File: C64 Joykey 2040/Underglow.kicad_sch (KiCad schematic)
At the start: 19 parts, among them J3 LED_EN, Q1 2N3904

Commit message: First layout drafted
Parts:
- J3: footprint TestPoint:TestPoint_Pad_D1.0mm -> TestPoint:TestPoint_THTPad_D1.5mm_Drill0.7mm
- Q1: footprint 2n3904:2N3904_TO-92_Horizontal_FlatSideDown -> Package_TO_SOT_THT:TO-92_Inline_Wide
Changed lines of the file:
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@@
 			)
 		)
-		(property "Footprint" "2n3904:2N3904_TO-92_Horizontal_FlatSideDown"
+		(property "Footprint" "Package_TO_SOT_THT:TO-92_Inline_Wide"
 			(at 186.69 109.855 0)
 			(effects
@@
 			)
 		)
-		(property "Footprint" "TestPoint:TestPoint_Pad_D1.0mm"
+		(property "Footprint" "TestPoint:TestPoint_THTPad_D1.5mm_Drill0.7mm"
 			(at 217.17 107.95 0)
 			(effects

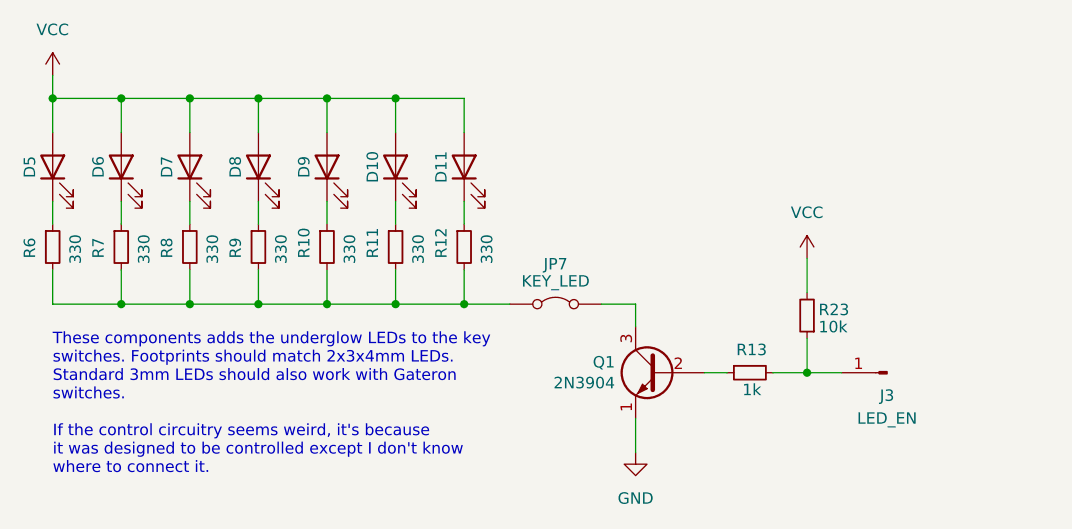
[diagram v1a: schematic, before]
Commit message: Try adding underglow to GPIO15
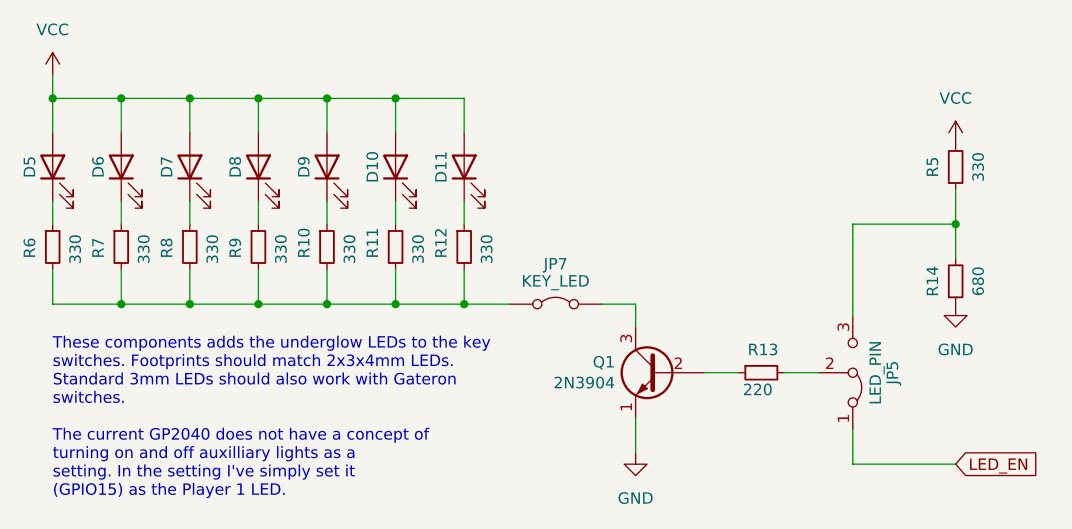
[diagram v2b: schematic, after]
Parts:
- removed J3: LED_EN, TestPoint:TestPoint_THTPad_D1.5mm_Drill0.7mm, symbol Connector:Conn_01x01_Pin
- removed R23: 10k, Resistor_THT:R_Axial_DIN0207_L6.3mm_D2.5mm_P10.16mm_Horizontal, symbol Device:R_Small
- added JP5: LED_PIN, Connector_PinHeader_2.54mm:PinHeader_1x03_P2.54mm_Vertical, symbol Jumper:Jumper_3_Bridged12
- added R14: 680, Resistor_THT:R_Axial_DIN0207_L6.3mm_D2.5mm_P10.16mm_Horizontal, symbol Device:R_Small
- added R5: 330, Resistor_THT:R_Axial_DIN0207_L6.3mm_D2.5mm_P10.16mm_Horizontal, symbol Device:R_Small
- R13: value 1k -> 220
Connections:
- net GND: now also R14.1
- net VCC: now also R5.2
- net at R13.2: now also JP5.2 (C)
- new net: JP5.3 (B), R14.2, R5.1
- new net LED_EN: JP5.1 (A)
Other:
- note added: "These components adds the underglow LEDs to the key switches. Footprints should match 2x3x4mm LEDs. Standard 3mm LEDs should also work with Gateron switches. The current GP2040 does not have a concept of turning on and off auxilliary lights as a setting. In the setting I've simply set it (GPIO15) as the Player 1 LED."
- note removed: "These components adds the underglow LEDs to the key switches. Footprints should match 2x3x4mm LEDs. Standard 3mm LEDs should also work with Gateron switches. If the control circuitry seems weird, it's because it was designed to be controlled except I don't know where to connect it."
- moved on the sheet: R13
